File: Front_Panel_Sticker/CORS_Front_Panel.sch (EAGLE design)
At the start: 9 parts

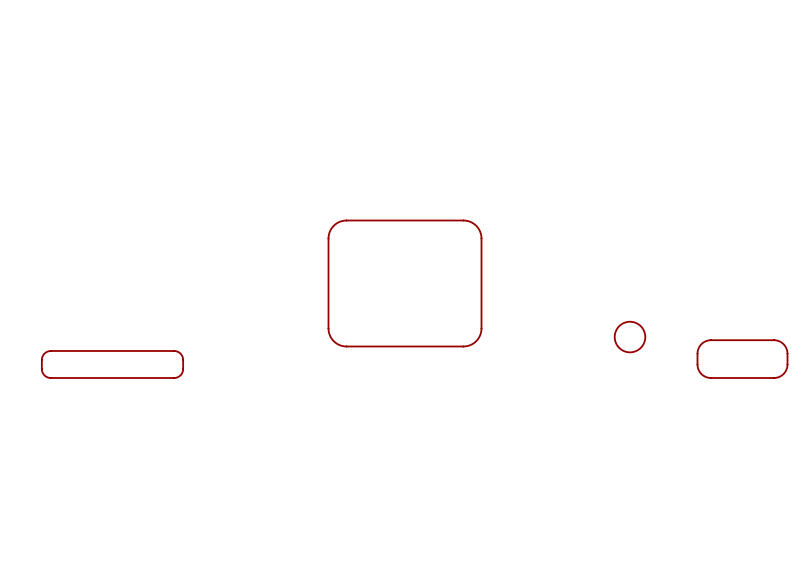
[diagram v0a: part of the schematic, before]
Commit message: Update OLED and Ethernet
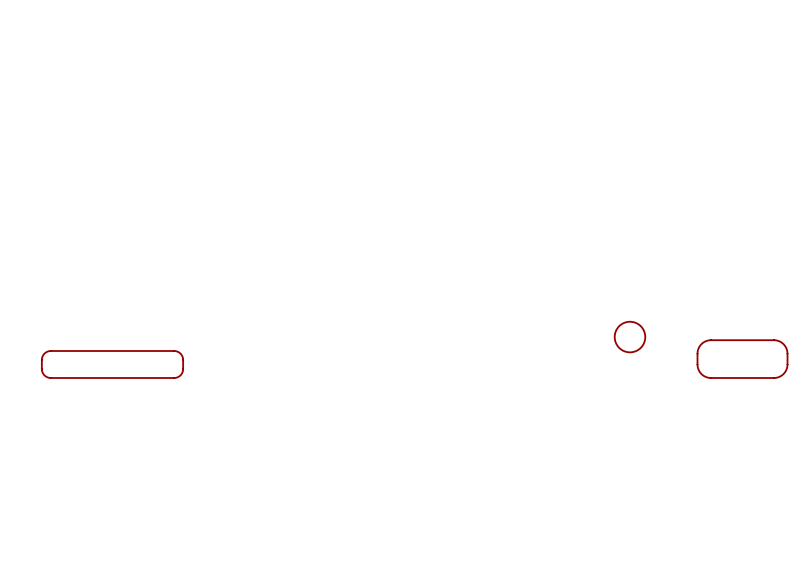
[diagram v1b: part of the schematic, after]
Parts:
- removed OLED: OLED, CORS_Panels:OLED
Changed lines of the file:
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@@
 <part name="ESP32_USB" library="CORS_Panels" deviceset="USB-C" device=""/>
 <part name="GNSS_USB" library="CORS_Panels" deviceset="USB-C" device=""/>
-<part name="OLED" library="CORS_Panels" deviceset="OLED" device=""/>
 <part name="LOGO1" library="SparkFun-Aesthetics" deviceset="SFE_LOGO_NAME_FLAME" device=".3_INCH" value="SFE_LOGO_NAME_FLAME.3_INCH"/>
 </parts>
@@
 <instance part="ESP32_USB" gate="G$1" x="162.5" y="95" smashed="yes"/>
 <instance part="GNSS_USB" gate="G$1" x="182.5" y="95" smashed="yes"/>
-<instance part="OLED" gate="G$1" x="125" y="105" smashed="yes"/>
 <instance part="LOGO1" gate="G$1" x="85" y="2.5" smashed="yes"/>
 </instances>

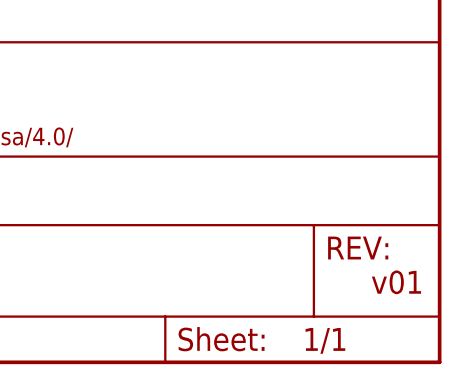
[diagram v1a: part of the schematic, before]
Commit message: Update stickers
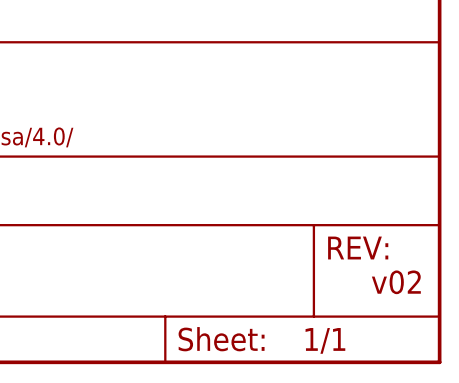
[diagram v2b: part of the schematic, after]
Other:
- note added: "v02"
- note removed: "v01"
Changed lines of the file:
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@@
 <sheet>
 <plain>
-<text x="241.3" y="7.62" size="2.54" layer="94" font="vector">v01</text>
+<text x="241.3" y="7.62" size="2.54" layer="94" font="vector">v02</text>
 <text x="167.64" y="10.16" size="2.54" layer="94" font="vector">Paul Clark</text>
 </plain>
